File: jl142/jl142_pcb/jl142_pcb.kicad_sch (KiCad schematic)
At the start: 44 parts, among them SW12 SWITCH_PUSH, SW13 SWITCH_PUSH, SW14 SWITCH_PUSH, SW17 SWITCH_PUSH, SW18 SWITCH_PUSH, SW19 SWITCH_PUSH, SW2 SWITCH_PUSH, SW20 SWITCH_PUSH, SW22 SWITCH_PUSH, SW23 SWITCH_PUSH, SW24 SWITCH_PUSH, SW25 SWITCH_PUSH, SW27 SWITCH_PUSH, SW28 SWITCH_PUSH, SW29 SWITCH_PUSH, SW3 SWITCH_PUSH, SW30 SWITCH_PUSH, SW34 SWITCH_PUSH, SW35 SWITCH_PUSH, SW36 SWITCH_PUSH, SW37 SWITCH_PUSH, SW39 SWITCH_PUSH, SW4 SWITCH_PUSH, SW40 SWITCH_PUSH, SW41 SWITCH_PUSH, SW42 SWITCH_PUSH, SW44 SWITCH_PUSH, SW45 SWITCH_PUSH, SW46 SWITCH_PUSH, SW47 SWITCH_PUSH, SW49 SWITCH_PUSH, SW50 SWITCH_PUSH, SW51 SWITCH_PUSH, SW54 SWITCH_PUSH, SW55 SWITCH_PUSH, SW56 SWITCH_PUSH, SW59 SWITCH_PUSH, SW60 SWITCH_PUSH, SW61 SWITCH_PUSH, SW7 SWITCH_PUSH, SW8 SWITCH_PUSH, SW9 SWITCH_PUSH, U1 ARDUINO_PRO_MICRO

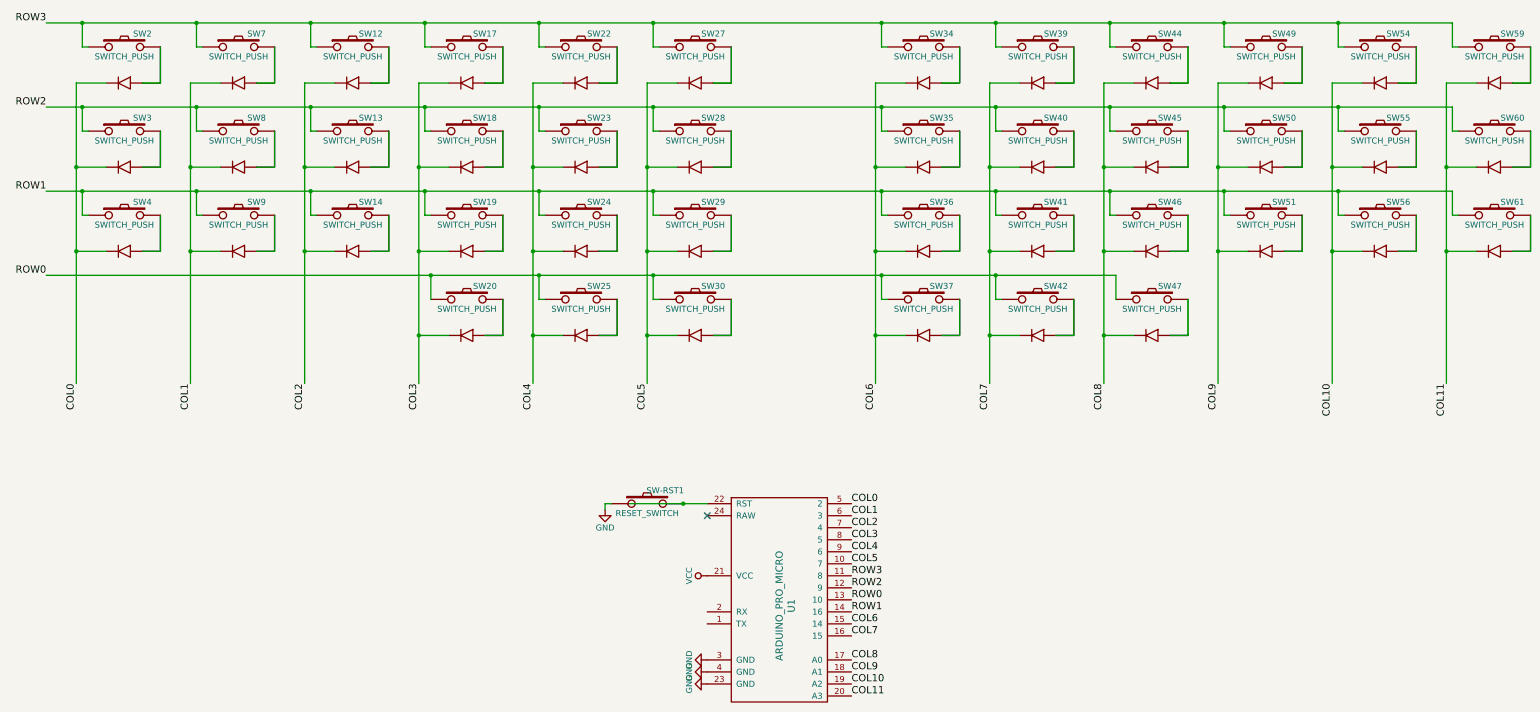
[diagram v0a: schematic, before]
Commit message: Changed the pro micro symbol.
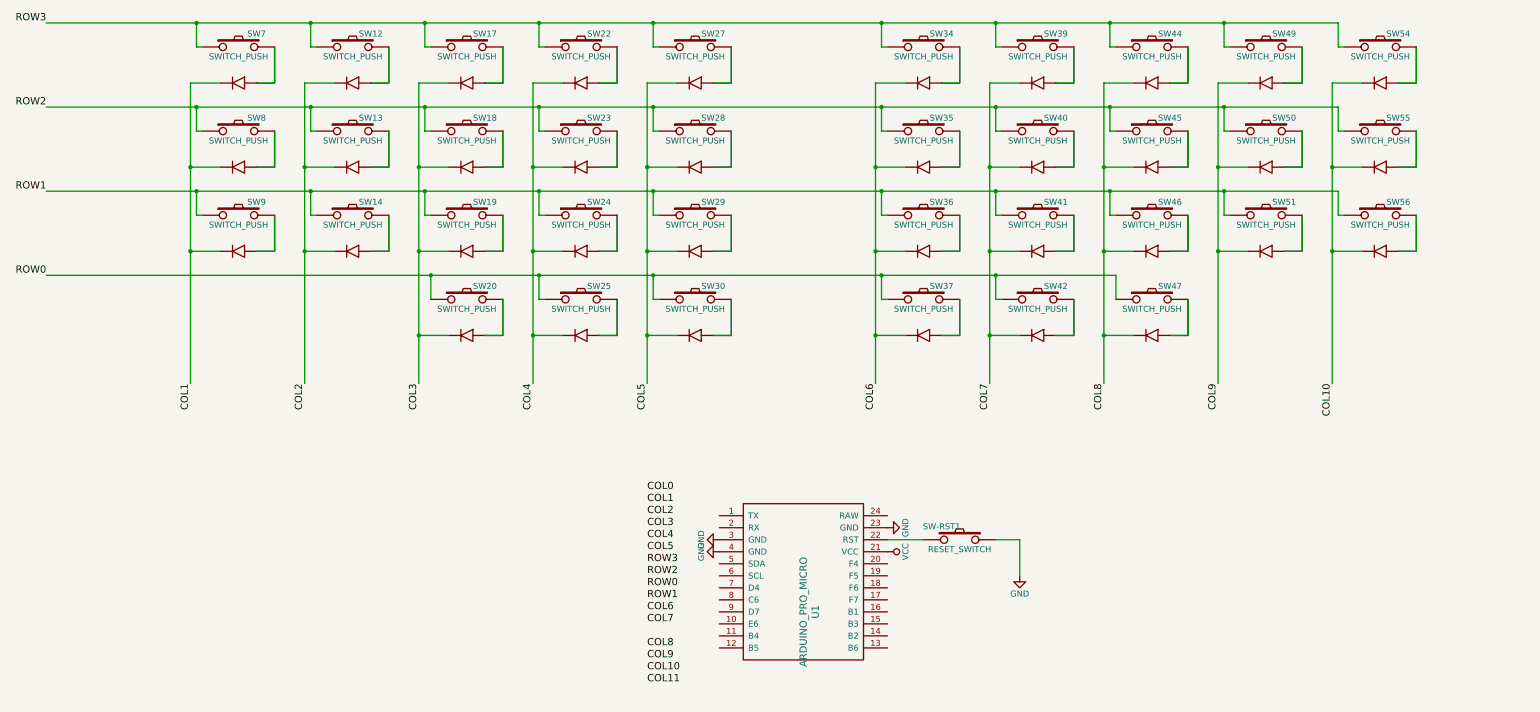
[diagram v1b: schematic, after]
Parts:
- removed SW2, SW3, SW4, SW59, SW60, SW61: SWITCH_PUSH, footprints:kailh_choc_with_diode, symbol symbols:SWITCH_WITH_DIODE
- U1: footprint footprints:ARDUINO_PRO_MICRO -> ProMicro_v2; symbol symbols:ARDUINO_PRO_MICRO -> symbols:ProMicro
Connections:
- net COL0: no longer U1.5 (2)
- net COL1: no longer U1.6 (3)
- net COL10: no longer U1.19 (A2)
- net COL11: no longer U1.20 (A3)
- net COL2: no longer U1.7 (4)
- net COL3: no longer U1.8 (5)
- net COL4: no longer U1.9 (6)
- net COL5: no longer U1.10 (7)
- net COL6: no longer U1.15 (14)
- net COL7: no longer U1.16 (15)
- net COL8: no longer U1.17 (A0)
- net COL9: no longer U1.18 (A1)
- net ROW0: no longer U1.13 (10)
- net ROW1: no longer U1.14 (16)
- net ROW2: no longer U1.12 (9)
- net ROW3: no longer U1.11 (8)
- no-connect marks 1 -> 0
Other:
- moved on the sheet: SW-RST1, U1

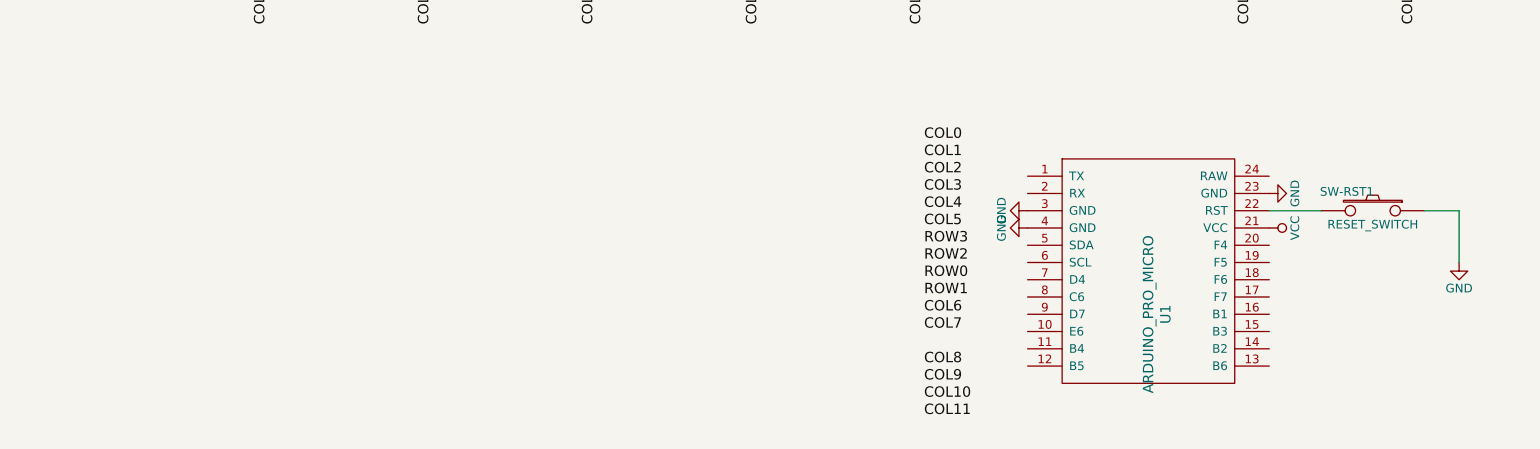
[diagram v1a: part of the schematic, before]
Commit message: Routed rev2 of jl142.
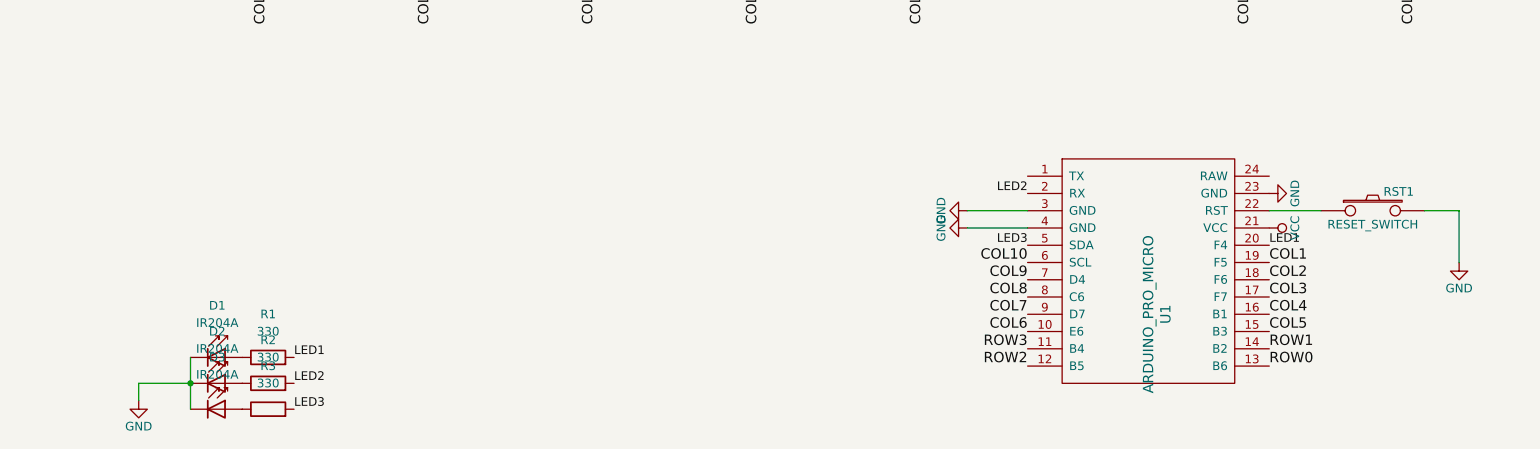
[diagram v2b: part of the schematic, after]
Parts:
- added D1, D2, D3: IR204A, LED_THT:LED_D3.0mm_IRBlack, symbol LED:IR204A
- added R1, R2, R3: 330, Resistor_THT:R_Axial_DIN0207_L6.3mm_D2.5mm_P7.62mm_Horizontal, symbol Device:R
- SW12, SW13, SW14, SW17, SW18, SW19, SW20, SW22, SW23, SW24, SW25, SW27, SW28, SW29, SW30, SW34, SW35, SW36, SW37, SW39, SW40, SW41, SW42, SW44, SW45, SW46, SW47, SW49, SW50, SW51, SW54, SW55, SW56, SW7, SW8, SW9: footprint footprints:kailh_choc_with_diode -> footprints:cherry_hotswap_with_diode
- U1: footprint ProMicro_v2 -> footprints:ARDUINO_PRO_MICRO
- renumbered SW-RST1 to RST1
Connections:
- net COL1: now also U1.19 (F5)
- net COL10: now also U1.6 (SCL)
- net COL2: now also U1.18 (F6)
- net COL3: now also U1.17 (F7)
- net COL4: now also U1.16 (B1)
- net COL5: now also U1.15 (B3)
- net COL6: now also U1.10 (E6)
- net COL7: now also U1.9 (D7)
- net COL8: now also U1.8 (C6)
- net COL9: now also U1.7 (D4)
- net GND: now also RST1.2, D1.1 (K), D2.1 (K), D3.1 (K); no longer RST1.1
- net ROW0: now also U1.13 (B6)
- net ROW1: now also U1.14 (B2)
- net ROW2: now also U1.12 (B5)
- net ROW3: now also U1.11 (B4)
- net LED2: now reaches U1.2 (RX)
- net LED2: now also R2.2
- net LED1: now reaches U1.20 (F4)
- net LED1: now also R1.2
- net at U1.22 (RST): now also RST1.1; no longer RST1.2
- net LED3: now reaches U1.5 (SDA)
- net LED3: now also R3.2
- new net: D1.2 (A), R1.1
- new net: D3.2 (A), R3.1
- new net: D2.2 (A), R2.1
